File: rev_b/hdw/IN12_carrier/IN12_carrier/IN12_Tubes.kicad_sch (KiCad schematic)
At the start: 8 parts

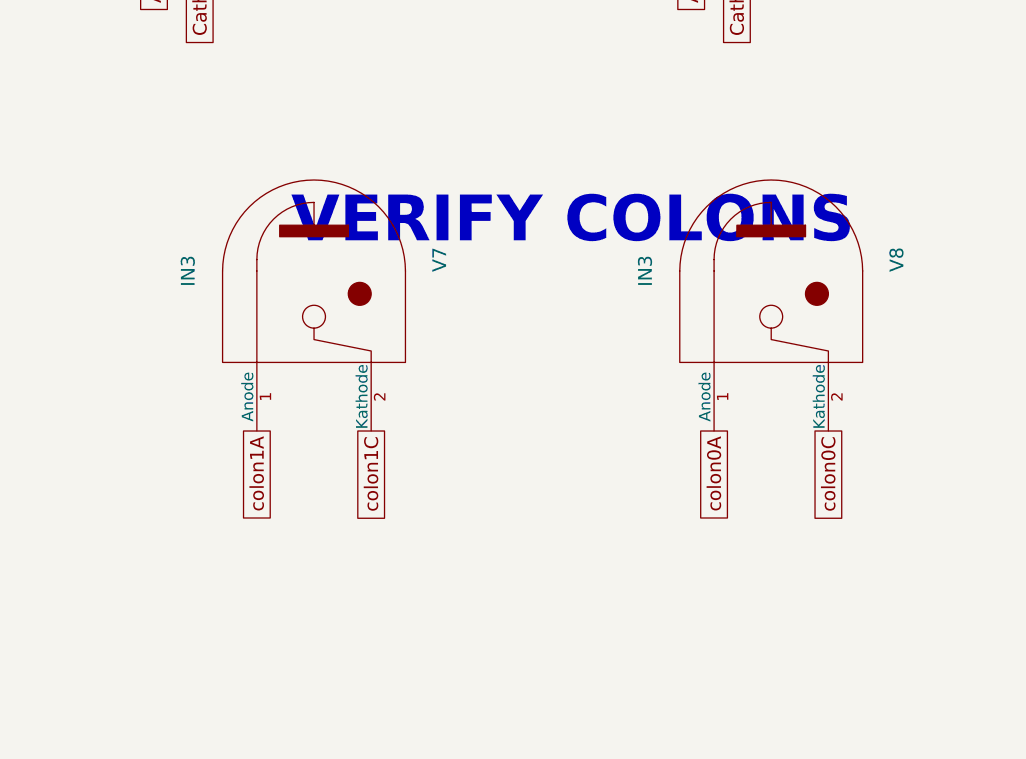
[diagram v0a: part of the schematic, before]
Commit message: updated footprints, ran some DRC
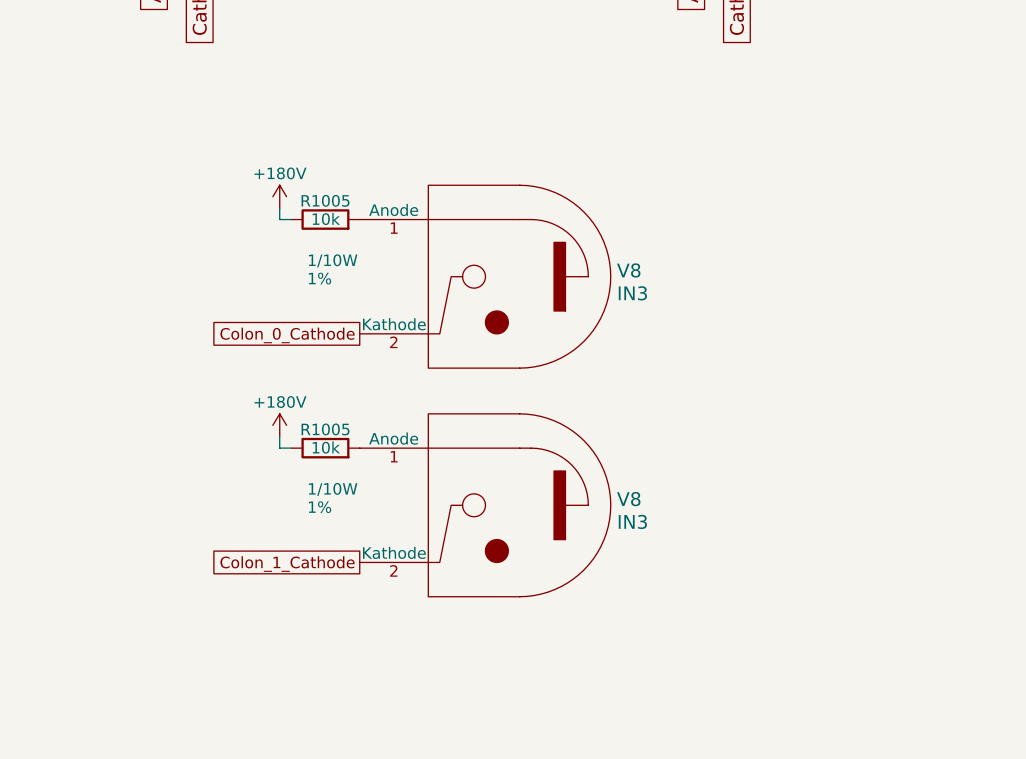
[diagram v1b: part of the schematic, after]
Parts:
- removed V7: IN3, LEDs:LED_D5.0mm, symbol Nixie-Test-rescue:IN3
- added R1005 (x2): 10k, Resistors_SMD:R_0603, symbol Nixie-Clock-rescue:R
- added V8: IN3, symbol Nixie-Test-rescue:IN3
- V8: footprint LEDs:LED_D5.0mm -> (none)
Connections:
- net colon0A: no longer names the net of V8.1 (Anode)
- net colon0A: now also R1005.2
- net colon0C renamed Colon_0_Cathode
- new net: R1005.2, V8.1 (Anode)
- new net +180V: R1005.1, R1005.1
- new net Colon_1_Cathode: V8.2 (Kathode)
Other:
- note removed: "VERIFY COLONS"
- moved on the sheet: V8

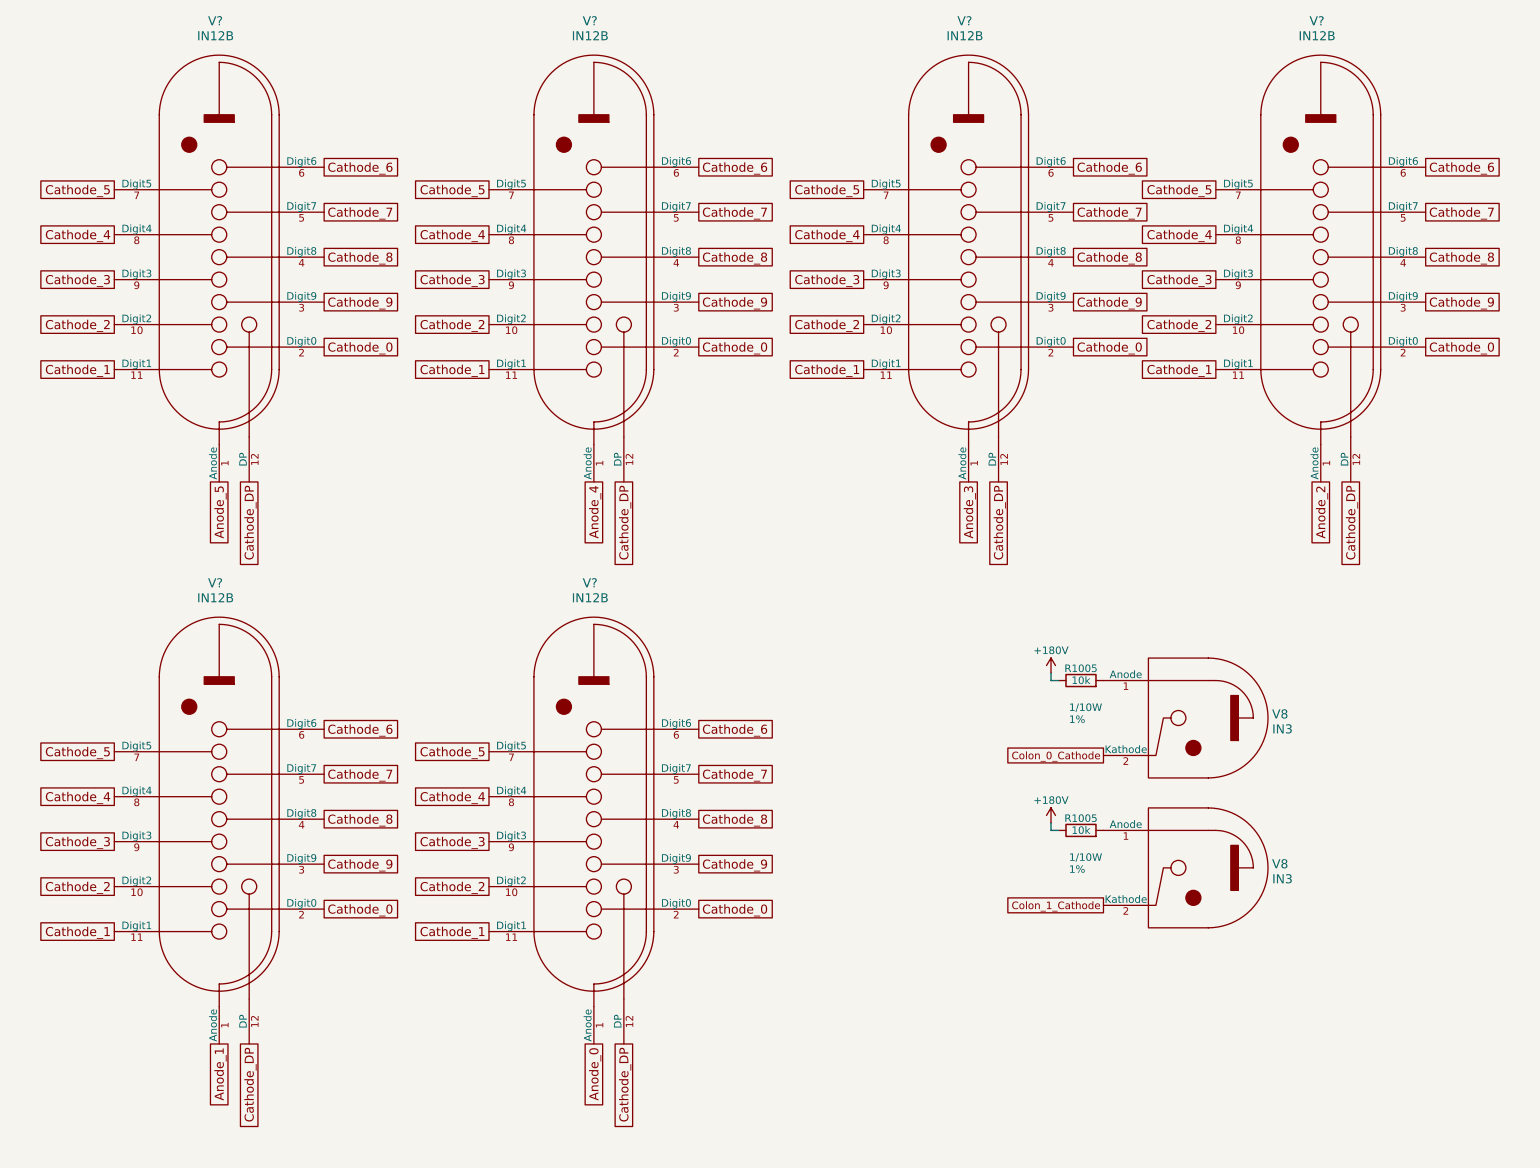
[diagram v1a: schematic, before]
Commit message: annotated, started arranging parts for IN12 carrier
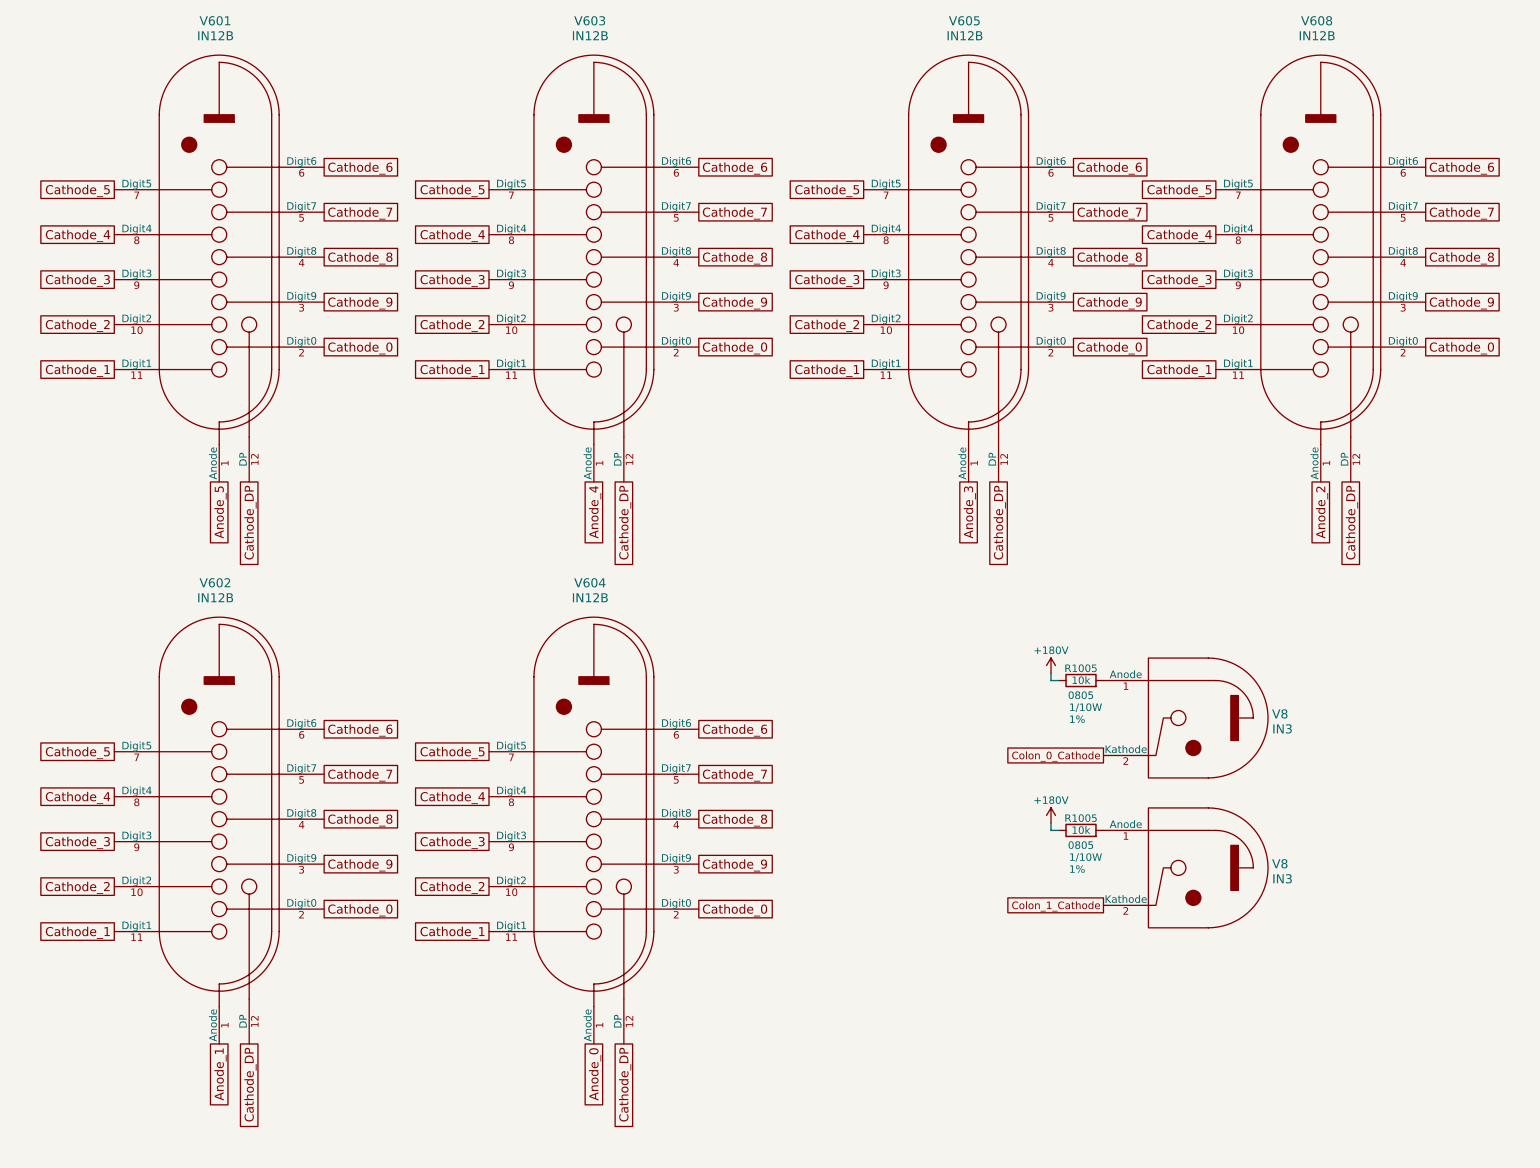
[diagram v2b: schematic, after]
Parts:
- R1005: footprint Resistors_SMD:R_0603 -> Resistors_SMD:R_0805; display_footprint 0603 -> 0805
- gave numbers to parts that had none: 6
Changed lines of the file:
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@@
   (symbol (lib_id "Custom Library:IN12B") (at 176.53 54.61 0) (unit 1)
     (in_bom yes) (on_board yes) (dnp no)
-    (property "Reference" "V?" (at 174.625 14.605 0)
+    (property "Reference" "V605" (at 174.625 14.605 0)
       (effects (font (size 1.524 1.524)))
     )
@@
       (project "IN12_carrier"
         (path "/c4d83a5b-e6ae-4326-9df5-0c4ac01f7d8c/364ea03e-c5ca-4ec9-aca8-c88c22a6aee2"
-          (reference "V?") (unit 1)
+          (reference "V605") (unit 1)
         )
       )
@@
       (project "IN12_carrier"
         (path "/c4d83a5b-e6ae-4326-9df5-0c4ac01f7d8c/364ea03e-c5ca-4ec9-aca8-c88c22a6aee2"
-          (reference "V?") (unit 1)
+          (reference "V606") (unit 1)
         )
       )
@@
   (symbol (lib_id "Custom Library:IN12B") (at 113.03 149.86 0) (unit 1)
     (in_bom yes) (on_board yes) (dnp no)
-    (property "Reference" "V?" (at 111.125 109.855 0)
+    (property "Reference" "V604" (at 111.125 109.855 0)
       (effects (font (size 1.524 1.524)))
     )
@@
       (project "IN12_carrier"
         (path "/c4d83a5b-e6ae-4326-9df5-0c4ac01f7d8c/364ea03e-c5ca-4ec9-aca8-c88c22a6aee2"
-          (reference "V?") (unit 1)
+          (reference "V604") (unit 1)
         )
       )
@@
       (effects (font (size 1.27 1.27)))
     )
-    (property "Footprint" "Resistors_SMD:R_0603" (at 191.77 132.715 0)
+    (property "Footprint" "Resistors_SMD:R_0805" (at 191.77 132.715 0)
       (effects (font (size 1.27 1.27)) (justify left) hide)
     )
@@
       (effects (font (size 1.27 1.27)) (justify right))
     )
-    (property "display_footprint" "0603" (at 194.31 126.365 0)
-      (effects (font (size 1.27 1.27)) hide)
+    (property "display_footprint" "0805" (at 194.31 128.905 90)
+      (effects (font (size 1.27 1.27)))
     )
     (pin "1")
@@
         )
         (path "/c4d83a5b-e6ae-4326-9df5-0c4ac01f7d8c/364ea03e-c5ca-4ec9-aca8-c88c22a6aee2"
-          (reference "R?") (unit 1)
+          (reference "R601") (unit 1)
         )
       )
@@
   (symbol (lib_id "Custom Library:IN12B") (at 49.53 149.86 0) (unit 1)
     (in_bom yes) (on_board yes) (dnp no)
-    (property "Reference" "V?" (at 47.625 109.855 0)
+    (property "Reference" "V602" (at 47.625 109.855 0)
       (effects (font (size 1.524 1.524)))
     )
@@
       (project "IN12_carrier"
         (path "/c4d83a5b-e6ae-4326-9df5-0c4ac01f7d8c/364ea03e-c5ca-4ec9-aca8-c88c22a6aee2"
-          (reference "V?") (unit 1)
+          (reference "V602") (unit 1)
         )
       )
@@
       (effects (font (size 1.27 1.27)))
     )
-    (property "Footprint" "Resistors_SMD:R_0603" (at 191.77 158.115 0)
+    (property "Footprint" "Resistors_SMD:R_0805" (at 191.77 158.115 0)
       (effects (font (size 1.27 1.27)) (justify left) hide)
     )
@@
       (effects (font (size 1.27 1.27)) (justify right))
     )
-    (property "display_footprint" "0603" (at 194.31 151.765 0)
-      (effects (font (size 1.27 1.27)) hide)
+    (property "display_footprint" "0805" (at 194.31 154.305 90)
+      (effects (font (size 1.27 1.27)))
     )
     (pin "1")
@@
         )
         (path "/c4d83a5b-e6ae-4326-9df5-0c4ac01f7d8c/364ea03e-c5ca-4ec9-aca8-c88c22a6aee2"
-          (reference "R?") (unit 1)
+          (reference "R602") (unit 1)
         )
       )
@@
       (project "IN12_carrier"
         (path "/c4d83a5b-e6ae-4326-9df5-0c4ac01f7d8c/364ea03e-c5ca-4ec9-aca8-c88c22a6aee2"
-          (reference "V?") (unit 1)
+          (reference "V607") (unit 1)
         )
       )
@@
   (symbol (lib_id "Custom Library:IN12B") (at 49.53 54.61 0) (unit 1)
     (in_bom yes) (on_board yes) (dnp no)
-    (property "Reference" "V?" (at 47.625 14.605 0)
+    (property "Reference" "V601" (at 47.625 14.605 0)
       (effects (font (size 1.524 1.524)))
     )
@@
       (project "IN12_carrier"
         (path "/c4d83a5b-e6ae-4326-9df5-0c4ac01f7d8c/364ea03e-c5ca-4ec9-aca8-c88c22a6aee2"
-          (reference "V?") (unit 1)
+          (reference "V601") (unit 1)
         )
       )
@@
   (symbol (lib_id "Custom Library:IN12B") (at 236.22 54.61 0) (unit 1)
     (in_bom yes) (on_board yes) (dnp no)
-    (property "Reference" "V?" (at 234.315 14.605 0)
+    (property "Reference" "V608" (at 234.315 14.605 0)
       (effects (font (size 1.524 1.524)))
     )
@@
       (project "IN12_carrier"
         (path "/c4d83a5b-e6ae-4326-9df5-0c4ac01f7d8c/364ea03e-c5ca-4ec9-aca8-c88c22a6aee2"
-          (reference "V?") (unit 1)
+          (reference "V608") (unit 1)
         )
       )
@@
   (symbol (lib_id "Custom Library:IN12B") (at 113.03 54.61 0) (unit 1)
     (in_bom yes) (on_board yes) (dnp no)
-    (property "Reference" "V?" (at 111.125 14.605 0)
+    (property "Reference" "V603" (at 111.125 14.605 0)
       (effects (font (size 1.524 1.524)))
     )
@@
       (project "IN12_carrier"
         (path "/c4d83a5b-e6ae-4326-9df5-0c4ac01f7d8c/364ea03e-c5ca-4ec9-aca8-c88c22a6aee2"
-          (reference "V?") (unit 1)
-        )
-      )
+          (reference "V603") (unit 1)
+        )
+      )

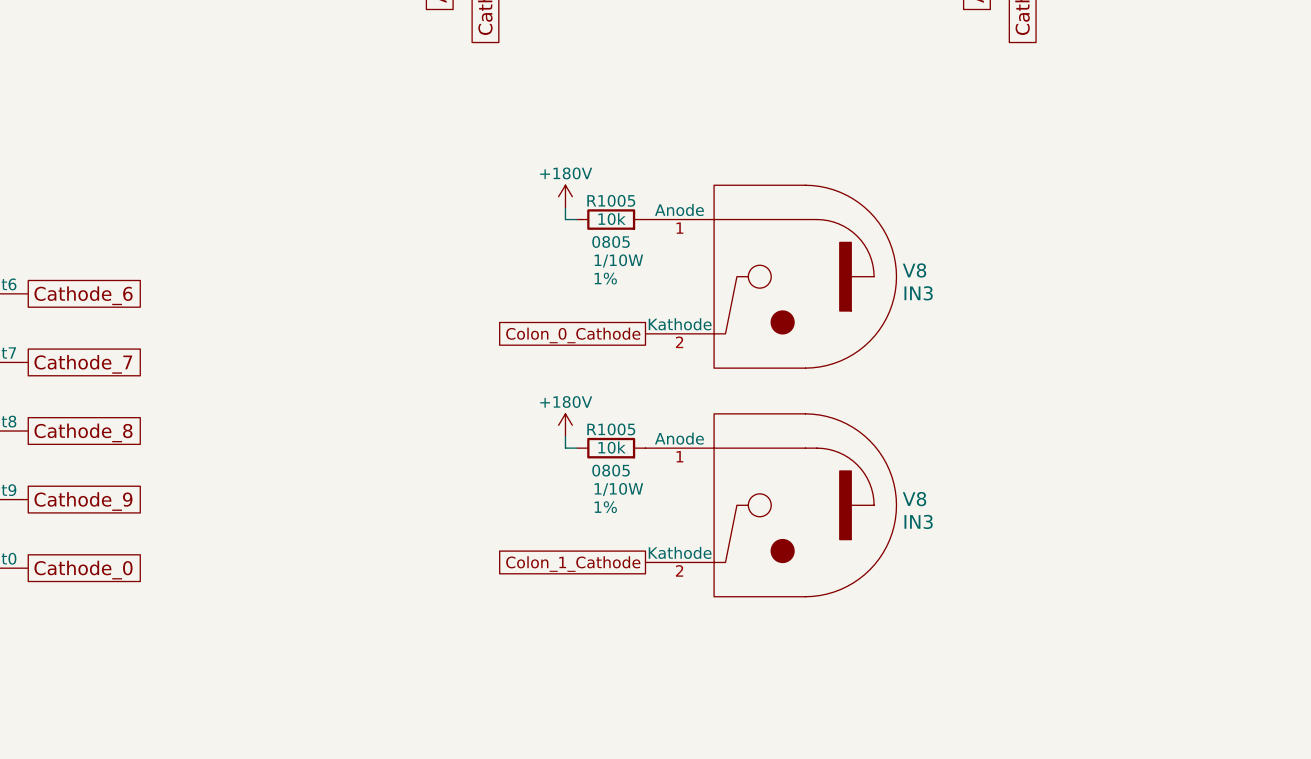
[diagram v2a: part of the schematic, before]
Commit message: lots of placement progress on IN12 carrier board
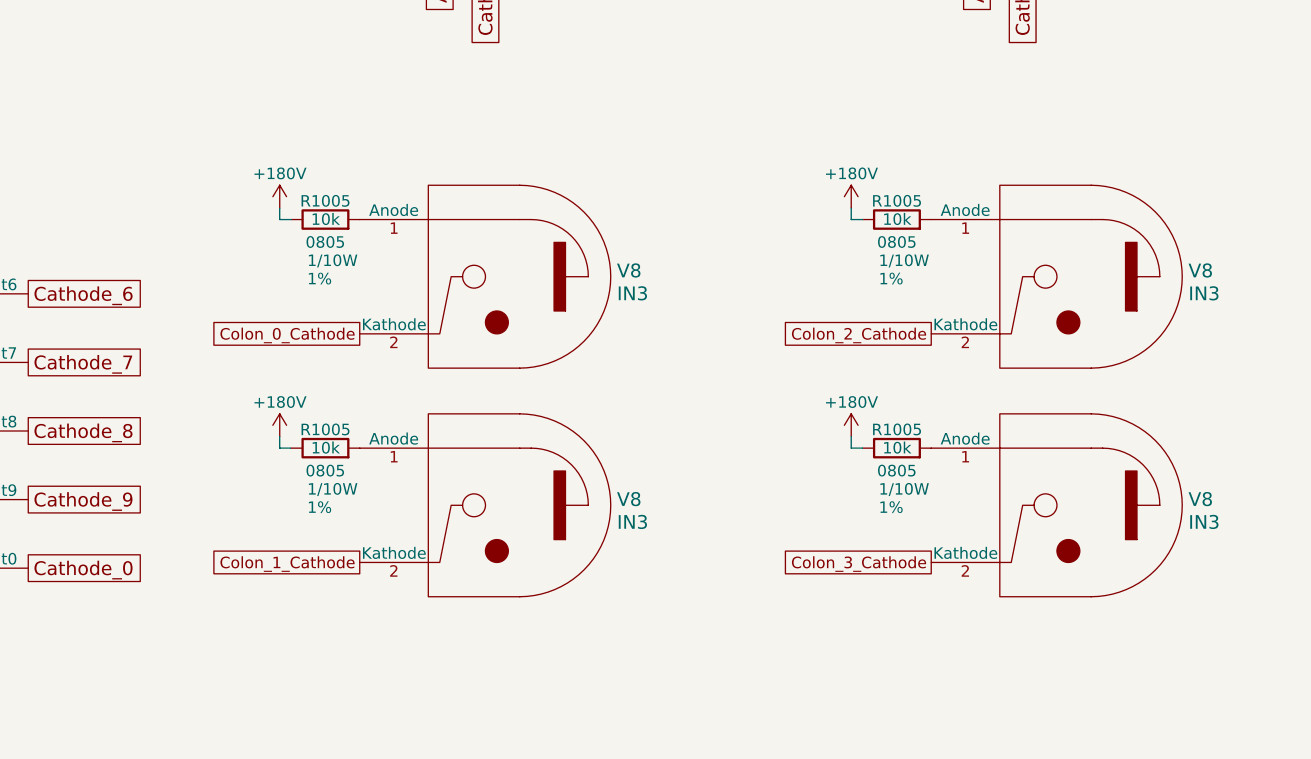
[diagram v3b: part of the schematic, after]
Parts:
- added R1005 (x2): 10k, Resistors_SMD:R_0805, symbol Nixie-Clock-rescue:R
- added V8 (x2): IN3, LED_THT:LED_D5.0mm, symbol Nixie-Test-rescue:IN3
- V8: footprint (none) -> LED_THT:LED_D5.0mm
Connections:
- net +180V: now also R1005.1, R1005.1
- new net: R1005.2, V8.1 (Anode) (x2)
- new net Colon_2_Cathode: V8.2 (Kathode)
- new net Colon_3_Cathode: V8.2 (Kathode)
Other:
- moved on the sheet: R1005, V8
